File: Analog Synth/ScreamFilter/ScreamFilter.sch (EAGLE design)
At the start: 39 parts, among them IC1 TL084D, IC2 TL082D, Q1 J310, Q2 J310, Q3 J310, Q5 J310

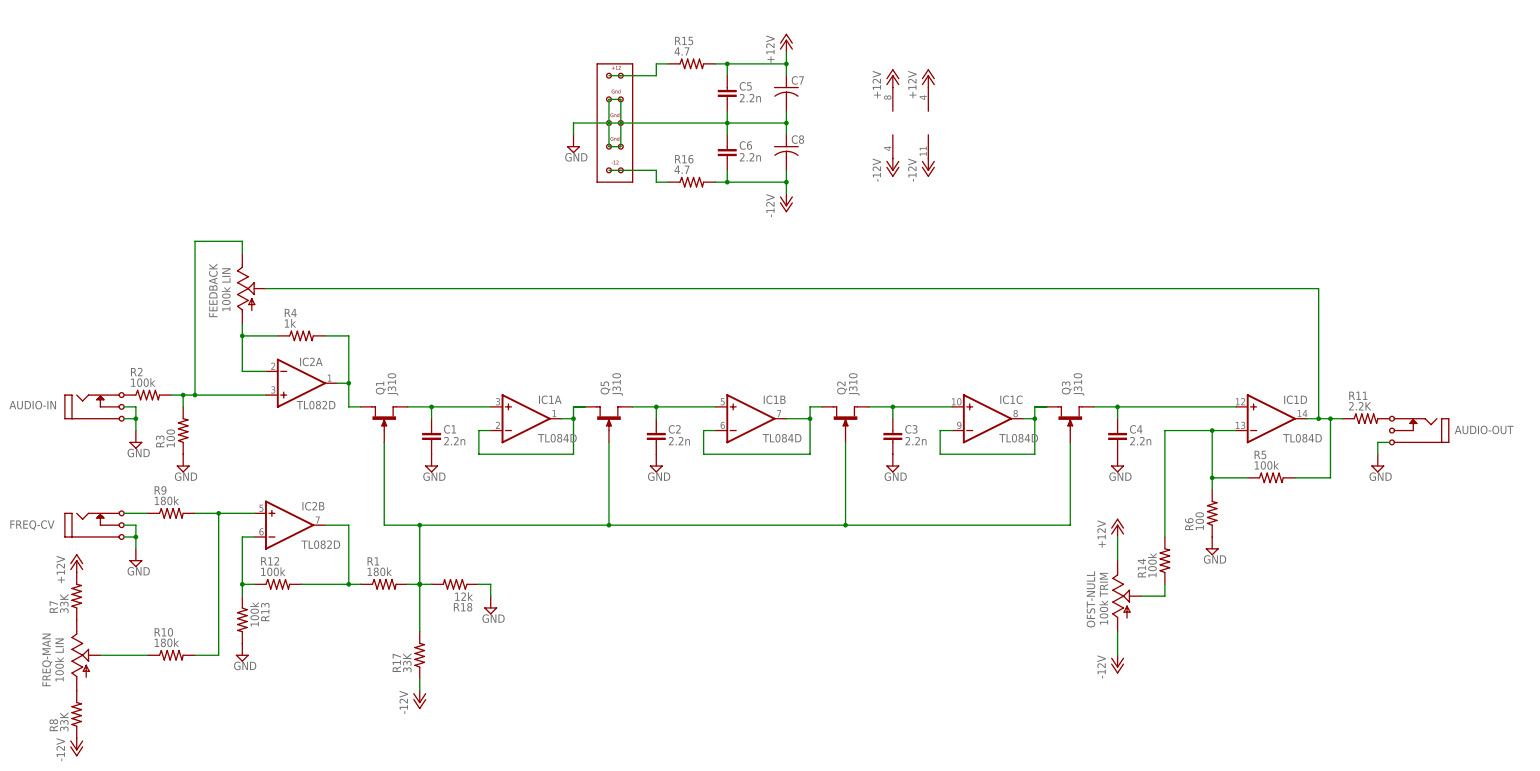
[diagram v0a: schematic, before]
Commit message: ScreamFilter v1.0; TODO: Add LEDs to ScreamFilter...   updated VCA-v2 for some reason.
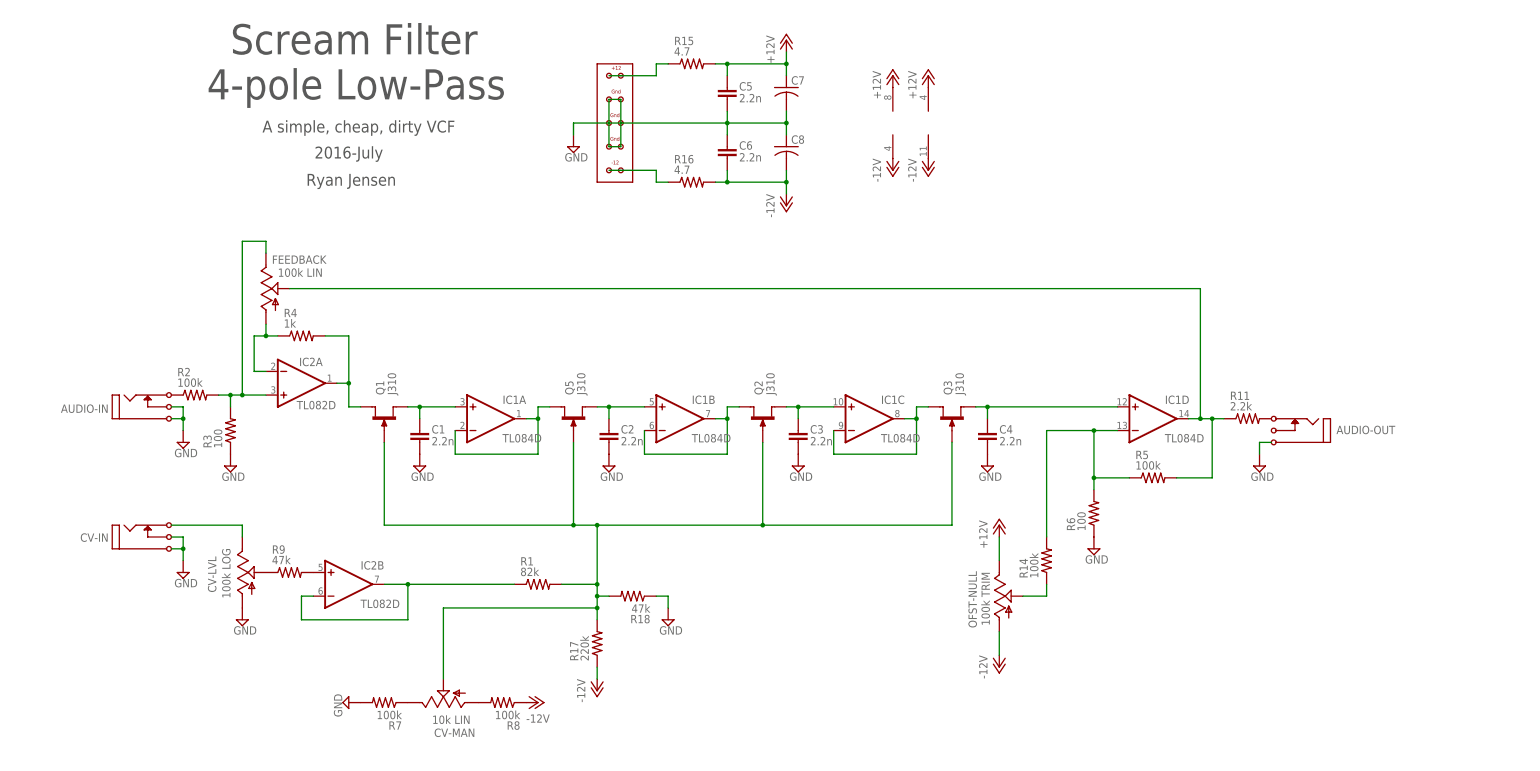
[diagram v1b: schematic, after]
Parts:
- removed FREQ-CV: I/O, !synth_sch:MONO_JACK
- removed FREQ-MAN: 100k LIN, pot:TRIM_US-B64Y
- removed R10: 180k, rcl:R-US_0204/7
- removed R12, R13: 100k, rcl:R-US_0204/7
- added CV-IN: I/O, !synth_sch:MONO_JACK
- added CV-LVL: 100k LOG, pot:TRIM_US-B64Y
- added CV-MAN: 10k LIN, pot:TRIM_US-B64Y
- R1: value 180k -> 82k
- R11: value 2.2K -> 2.2k
- R17: value 33K -> 220k
- R18: value 12k -> 47k
- R7, R8: value 33K -> 100k
- R9: value 180k -> 47k
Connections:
- removed net N$11: Q2.D
- removed net N$15: Q3.D
- removed net N$3: Q1.G, Q2.G, Q3.G, Q5.G, R1.2, R17.2, R18.2
- removed net N$7: Q5.D
- net +12V: no longer R7.2
- net GND: now also CV-IN.P$1, CV-IN.P3, CV-LVL.A, R7.2; no longer FREQ-CV.P$1, FREQ-CV.P3, R13.2
- net N$13: now also Q3.D
- net N$17: now also CV-MAN.E; no longer FREQ-MAN.E
- net N$20: now also CV-MAN.A; no longer FREQ-MAN.A
- net N$21: now also CV-IN.P2, CV-LVL.E; no longer FREQ-CV.P2, R9.1
- net N$22: no longer R10.2
- net N$23: now also CV-MAN.S, Q1.G, Q2.G, Q3.G, Q5.G, R1.2, R17.2, R18.2; no longer FREQ-MAN.S, R10.1
- net N$25: now also CV-LVL.S, R9.1; no longer IC2B.-IN, R12.1, R13.1
- net N$30: now also IC2B.-IN; no longer R12.2
- net N$6: now also Q5.D
- net N$9: now also Q2.D
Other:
- note added: "2016-July"
- note added: "A simple, cheap, dirty VCF"
- note added: "Ryan Jensen"
- note added: "Scream Filter 4-pole Low-Pass"
- moved on the sheet: AUDIO-IN, AUDIO-OUT, C1, C2, C3, C4, FEEDBACK, IC1A, IC1B, IC1C, IC1D, IC2B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

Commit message: VCA-v2 new schematic pdf; ScreamFilter layout has begun.
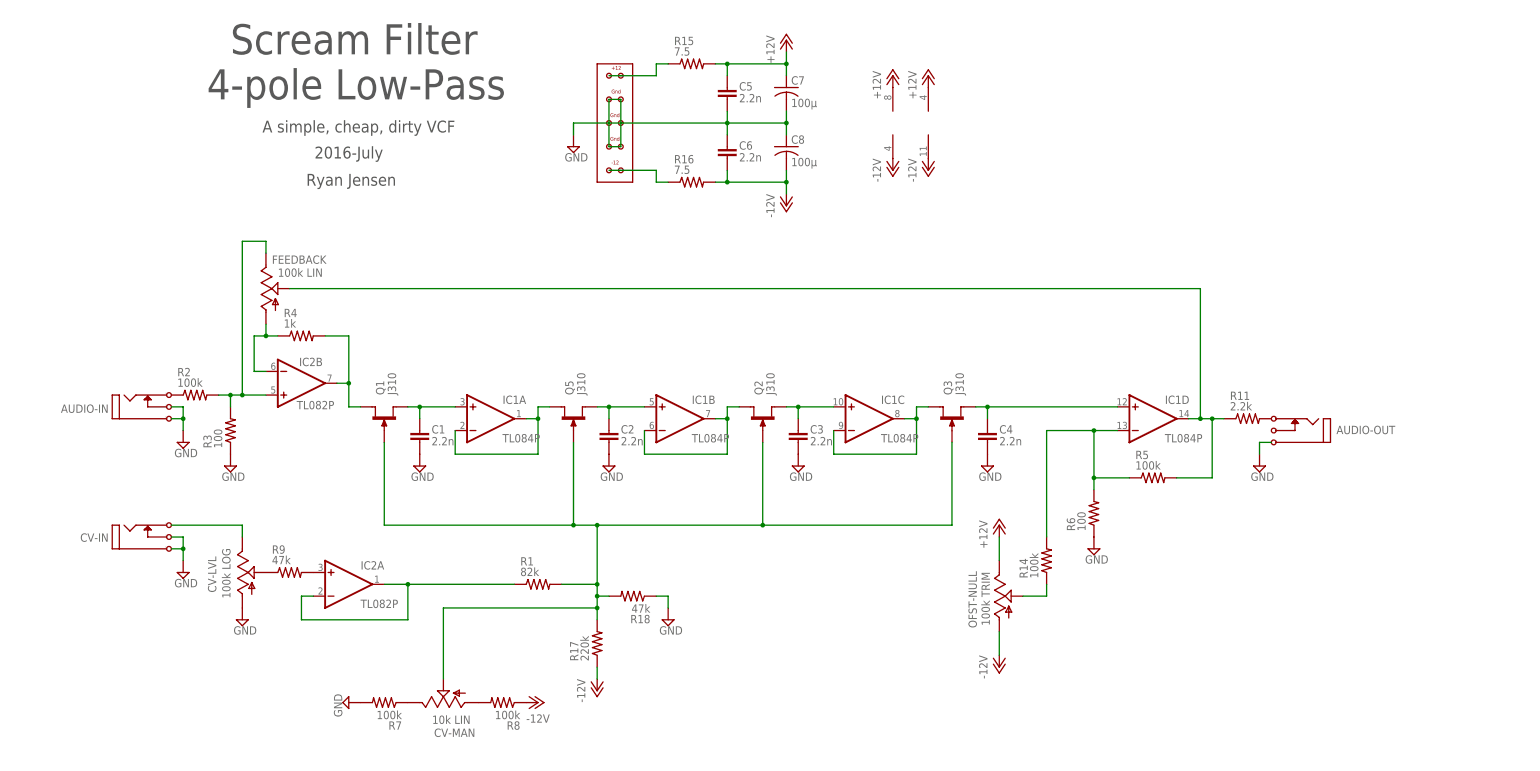
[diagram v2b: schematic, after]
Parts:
- C7, C8: value (none) -> 100µ
- IC1: value TL084D -> TL084P; device linear:TL084D -> linear:TL084P
- IC2: value TL082D -> TL082P; device linear:TL082D -> linear:TL082P
- R15, R16: value 4.7 -> 7.5
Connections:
- net N$2: now also IC2B.+IN; no longer IC2A.+IN
- net N$22: now also IC2A.+IN; no longer IC2B.+IN
- net N$27: now also IC2B.-IN; no longer IC2A.-IN
- net N$30: now also IC2A.-IN, IC2A.OUT; no longer IC2B.-IN, IC2B.OUT
- net N$4: now also IC2B.OUT; no longer IC2A.OUT
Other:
- moved on the sheet: IC2A, IC2B

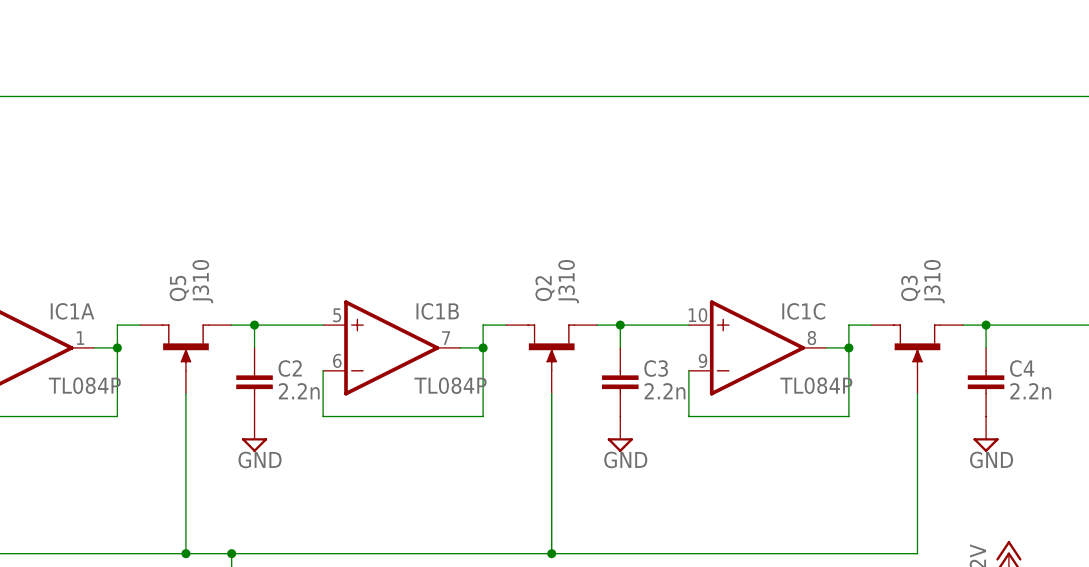
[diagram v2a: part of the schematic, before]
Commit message: working on ScreamFilter layout. close to finished
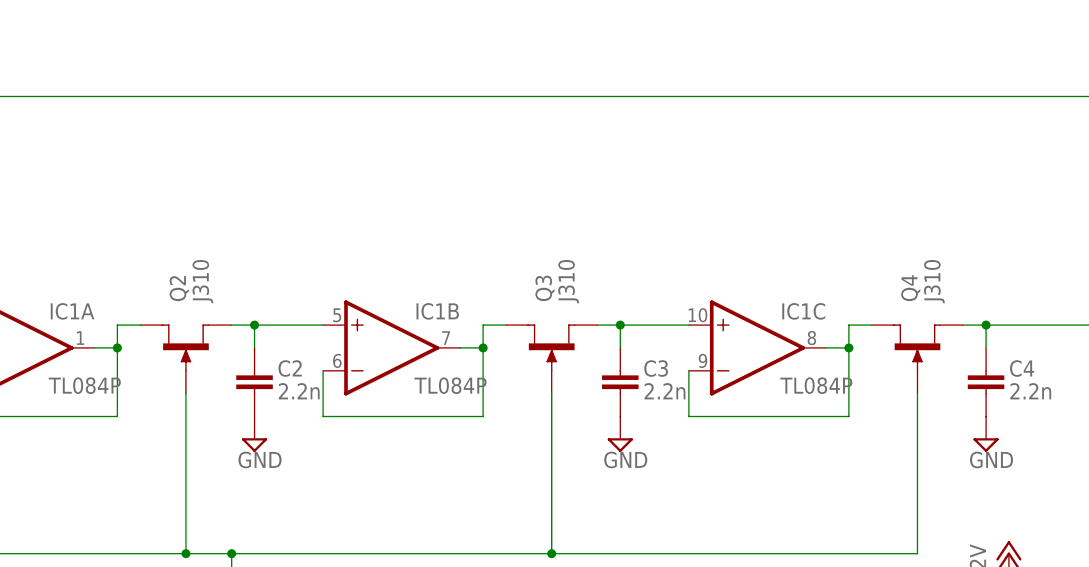
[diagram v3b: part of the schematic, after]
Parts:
- removed Q5: J310, transistor-small-signal:J310
- added Q4: J310, transistor-small-signal:J310
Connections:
- net N$12: now also Q3.S; no longer Q2.S
- net N$13: now also Q4.D; no longer Q3.D
- net N$16: now also Q4.S; no longer Q3.S
- net N$23: now also Q4.G; no longer Q5.G
- net N$6: now also Q2.D; no longer Q5.D
- net N$8: now also Q2.S; no longer Q5.S
- net N$9: now also Q3.D; no longer Q2.D
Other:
- moved on the sheet: Q2, Q3
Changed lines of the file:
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@@
 <part name="SUPPLY2" library="supply2" deviceset="GND" device=""/>
 <part name="R4" library="rcl" deviceset="R-US_" device="0204/7" value="1k"/>
-<part name="Q5" library="transistor-small-signal" deviceset="J310" device=""/>
+<part name="Q2" library="transistor-small-signal" deviceset="J310" device=""/>
 <part name="SUPPLY3" library="supply2" deviceset="GND" device=""/>
 <part name="C2" library="rcl" deviceset="C-EU" device="025-025X050" value="2.2n"/>
-<part name="Q2" library="transistor-small-signal" deviceset="J310" device=""/>
+<part name="Q3" library="transistor-small-signal" deviceset="J310" device=""/>
 <part name="SUPPLY4" library="supply2" deviceset="GND" device=""/>
 <part name="C3" library="rcl" deviceset="C-EU" device="025-025X050" value="2.2n"/>
-<part name="Q3" library="transistor-small-signal" deviceset="J310" device=""/>
+<part name="Q4" library="transistor-small-signal" deviceset="J310" device=""/>
 <part name="SUPPLY5" library="supply2" deviceset="GND" device=""/>
 <part name="C4" library="rcl" deviceset="C-EU" device="025-025X050" value="2.2n"/>
@@
 <instance part="SUPPLY2" gate="GND" x="-38.1" y="63.5"/>
 <instance part="R4" gate="G$1" x="-22.86" y="91.44"/>
-<instance part="Q5" gate="1" x="35.56" y="73.66" rot="R90"/>
+<instance part="Q2" gate="1" x="35.56" y="73.66" rot="R90"/>
 <instance part="SUPPLY3" gate="GND" x="43.18" y="63.5"/>
 <instance part="C2" gate="G$1" x="43.18" y="71.12"/>
-<instance part="Q2" gate="1" x="76.2" y="73.66" rot="R90"/>
+<instance part="Q3" gate="1" x="76.2" y="73.66" rot="R90"/>
 <instance part="SUPPLY4" gate="GND" x="83.82" y="63.5"/>
 <instance part="C3" gate="G$1" x="83.82" y="71.12"/>
-<instance part="Q3" gate="1" x="116.84" y="73.66" rot="R90"/>
+<instance part="Q4" gate="1" x="116.84" y="73.66" rot="R90"/>
 <instance part="SUPPLY5" gate="GND" x="124.46" y="63.5"/>
 <instance part="C4" gate="G$1" x="124.46" y="71.12"/>
@@
 <wire x1="27.94" y1="73.66" x2="27.94" y2="76.2" width="0.1524" layer="91"/>
 <junction x="27.94" y="73.66"/>
-<pinref part="Q5" gate="1" pin="D"/>
+<pinref part="Q2" gate="1" pin="D"/>
 <wire x1="30.48" y1="76.2" x2="27.94" y2="76.2" width="0.1524" layer="91"/>
 </segment>
@@
 <net name="N$8" class="0">
 <segment>
-<pinref part="Q5" gate="1" pin="S"/>
+<pinref part="Q2" gate="1" pin="S"/>
 <pinref part="C2" gate="G$1" pin="1"/>
 <wire x1="40.64" y1="76.2" x2="43.18" y2="76.2" width="0.1524" layer="91"/>
@@
 <junction x="68.58" y="73.66"/>
 <wire x1="68.58" y1="73.66" x2="68.58" y2="76.2" width="0.1524" layer="91"/>
-<pinref part="Q2" gate="1" pin="D"/>
+<pinref part="Q3" gate="1" pin="D"/>
 <wire x1="71.12" y1="76.2" x2="68.58" y2="76.2" width="0.1524" layer="91"/>
 </segment>
@@
 <net name="N$12" class="0">
 <segment>
-<pinref part="Q2" gate="1" pin="S"/>
+<pinref part="Q3" gate="1" pin="S"/>
 <pinref part="C3" gate="G$1" pin="1"/>
 <wire x1="81.28" y1="76.2" x2="83.82" y2="76.2" width="0.1524" layer="91"/>
@@
 <pinref part="IC1" gate="C" pin="OUT"/>
 <wire x1="109.22" y1="76.2" x2="111.76" y2="76.2" width="0.1524" layer="91"/>
-<pinref part="Q3" gate="1" pin="D"/>
+<pinref part="Q4" gate="1" pin="D"/>
 </segment>
 </net>
 <net name="N$16" class="0">
 <segment>
-<pinref part="Q3" gate="1" pin="S"/>
+<pinref part="Q4" gate="1" pin="S"/>
 <pinref part="C4" gate="G$1" pin="1"/>
 <wire x1="121.92" y1="76.2" x2="124.46" y2="76.2" width="0.1524" layer="91"/>
@@
 <wire x1="40.64" y1="35.56" x2="40.64" y2="38.1" width="0.1524" layer="91"/>
 <wire x1="-5.08" y1="68.58" x2="-5.08" y2="50.8" width="0.1524" layer="91"/>
-<pinref part="Q5" gate="1" pin="G"/>
+<pinref part="Q2" gate="1" pin="G"/>
 <wire x1="-5.08" y1="50.8" x2="35.56" y2="50.8" width="0.1524" layer="91"/>
 <wire x1="35.56" y1="68.58" x2="35.56" y2="50.8" width="0.1524" layer="91"/>
-<pinref part="Q2" gate="1" pin="G"/>
+<pinref part="Q3" gate="1" pin="G"/>
 <wire x1="35.56" y1="50.8" x2="40.64" y2="50.8" width="0.1524" layer="91"/>
 <wire x1="40.64" y1="50.8" x2="76.2" y2="50.8" width="0.1524" layer="91"/>
 <wire x1="76.2" y1="68.58" x2="76.2" y2="50.8" width="0.1524" layer="91"/>
-<pinref part="Q3" gate="1" pin="G"/>
+<pinref part="Q4" gate="1" pin="G"/>
 <wire x1="76.2" y1="50.8" x2="116.84" y2="50.8" width="0.1524" layer="91"/>
 <wire x1="116.84" y1="50.8" x2="116.84" y2="68.58" width="0.1524" layer="91"/>
